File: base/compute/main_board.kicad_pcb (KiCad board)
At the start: 2 copper layers, 66.5 x 44 mm, 42 parts, among them J1 USB_C_Receptacle_USB2.0_16P, J3 Conn_02x20_Counter_Clockwise, SW1 SW_Push_Open, SW2 SW_Push_Open, U1 MCP1700T-1202ETT, U2 ESP32-S3-WROOM-2, U3 LD1117S33TR_SOT223, U4 W25X20CLSN, U5 ICE40UP5K-SG48ITR-FPGA_Lattice

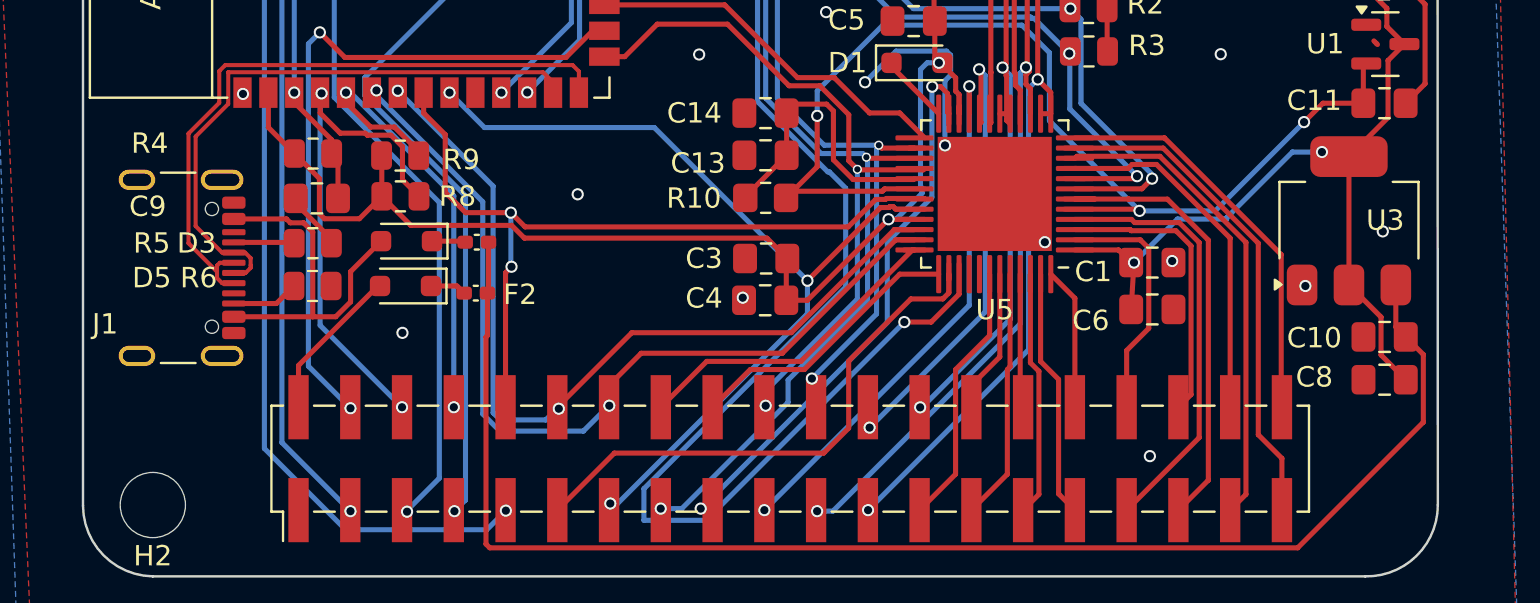
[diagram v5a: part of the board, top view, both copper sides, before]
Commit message: kicost integration for compute and extension
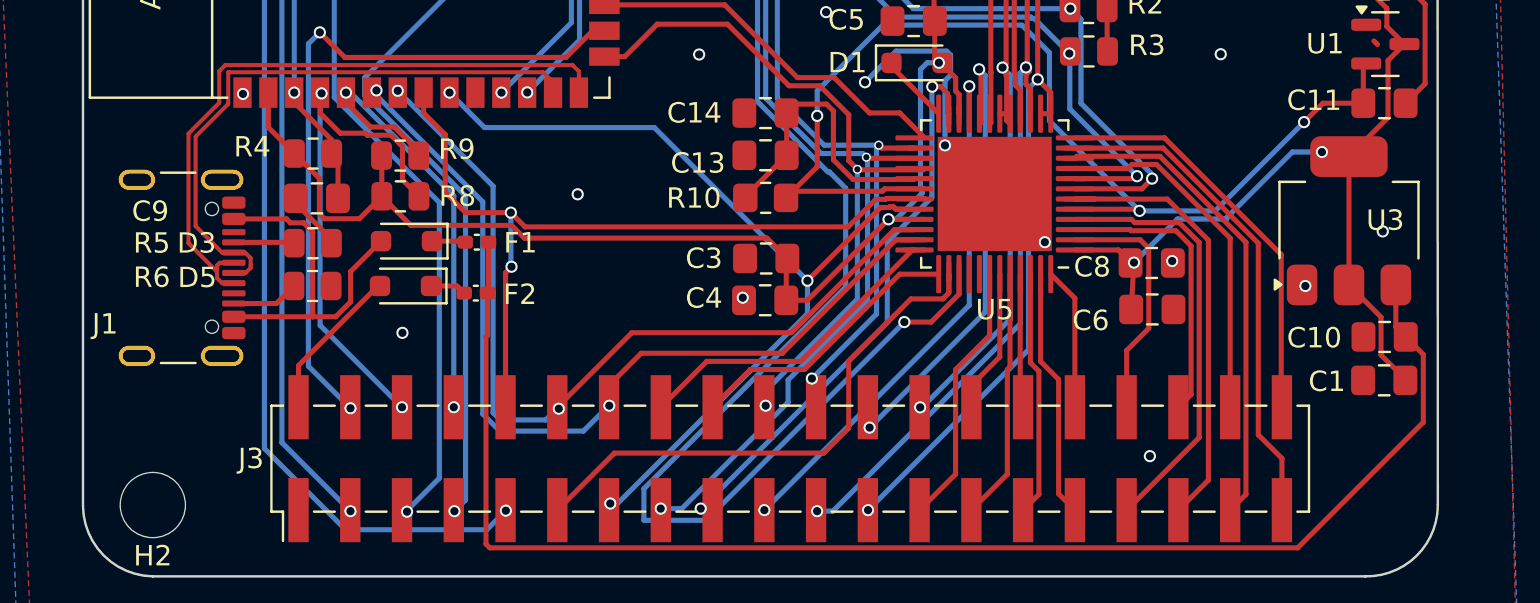
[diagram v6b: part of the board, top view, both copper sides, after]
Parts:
- moved C8 12.8 mm to (223.5, 159.1), turned to 0 degrees
- moved C1 12.8 mm to (234.9, 164.8), turned to 180 degrees
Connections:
- net FPGA41 renamed INDEX_X
- net GPIO43 renamed UART
- net GPIO44 renamed UARX
- J3 pad 1: unconnected-(J3-Pin_1-Pad1) -> GND
- J3 pad 11: HALL2 -> HALL2_old
- J3 pad 14: FPGA46 -> Z_STEP
- J3 pad 15: FPGA38 -> Z_DIR
- J3 pad 16: DIGITAL -> Y_DIR
- J3 pad 18: HALL1 -> Y_STEP
- J3 pad 19: Z_STEP -> Y_PO
- J3 pad 22: FPGA39 -> X_STEP
- J3 pad 24: Z_DIR -> X_DIR
- J3 pad 25: HALL3 -> X_PO
- J3 pad 27: uL -> FPGA3
- J3 pad 28: uH -> FPGA49
- J3 pad 29: vL -> DIGITAL
- J3 pad 30: vH -> HALL1
- J3 pad 31: wH -> HALL2
- J3 pad 32: wL -> HALL3
- J3 pad 33: X_DIR -> uH
- J3 pad 34: IC_HB_PWM1 -> uL
- J3 pad 35: X_STEP -> vH
- J3 pad 36: IC_HB_PWM2 -> vL
- J3 pad 37: Y_DIR -> wH
- J3 pad 38: X_PO -> wL
- J3 pad 39: Y_STEP -> IC_HB_PWM1
- J3 pad 40: Y_PO -> IC_HB_PWM2
- U2 pad 38: FPGA39 -> X_STEP
- U2 pad 39: FPGA38 -> Z_DIR
- U2 pad 6: FPGA46 -> Z_STEP
- U5 pad 10: Y_DIR -> wH
- U5 pad 11: Y_STEP -> IC_HB_PWM1
- U5 pad 12: Y_PO -> IC_HB_PWM2
- U5 pad 2: IC_HB_PWM1 -> uL
- U5 pad 20: Z_DIR -> X_DIR
- U5 pad 21: Z_STEP -> Y_PO
- U5 pad 26: FPGA39 -> X_STEP
- U5 pad 27: FPGA38 -> Z_DIR
- U5 pad 3: IC_HB_PWM2 -> vL
- U5 pad 35: FPGA46 -> Z_STEP
- U5 pad 36: DIGITAL -> Y_DIR
- U5 pad 37: HALL1 -> Y_STEP
- U5 pad 38: HALL2 -> HALL2_old
- U5 pad 4: X_DIR -> uH
- U5 pad 42: HALL3 -> X_PO
- U5 pad 43: uH -> FPGA49
- U5 pad 44: uL -> FPGA3
- U5 pad 45: vH -> HALL1
- U5 pad 46: vL -> DIGITAL
- U5 pad 47: wH -> HALL2
- U5 pad 48: wL -> HALL3
- U5 pad 6: X_STEP -> vH
- U5 pad 9: X_PO -> wL
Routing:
- net FPGA38: track 78.6 -> 0.00 mm, vias 3 -> 0
- net FPGA39: track 65.4 -> 0.00 mm, vias 3 -> 0
- net Z_DIR: track 22.8 -> 78.6 mm, vias 2 -> 3
- net FPGA46: track 45.3 -> 0.00 mm, vias 2 -> 0
- net X_STEP: track 22.7 -> 65.4 mm, vias 0 -> 3
- net HALL2_old: track 0.00 -> 27.2 mm
- net Z_STEP: track 26.3 -> 45.3 mm
- net vH: track 6.59 -> 22.7 mm
- net HALL2: track 27.2 -> 12.3 mm
- net uH: track 7.16 -> 21.2 mm
- net IC_HB_PWM1: track 12.0 -> 24.9 mm
- net FPGA3: track 0.00 -> 12.4 mm
- net wH: track 12.3 -> 24.1 mm
- net Y_STEP: track 24.9 -> 13.8 mm
- net wL: track 7.17 -> 18.1 mm
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
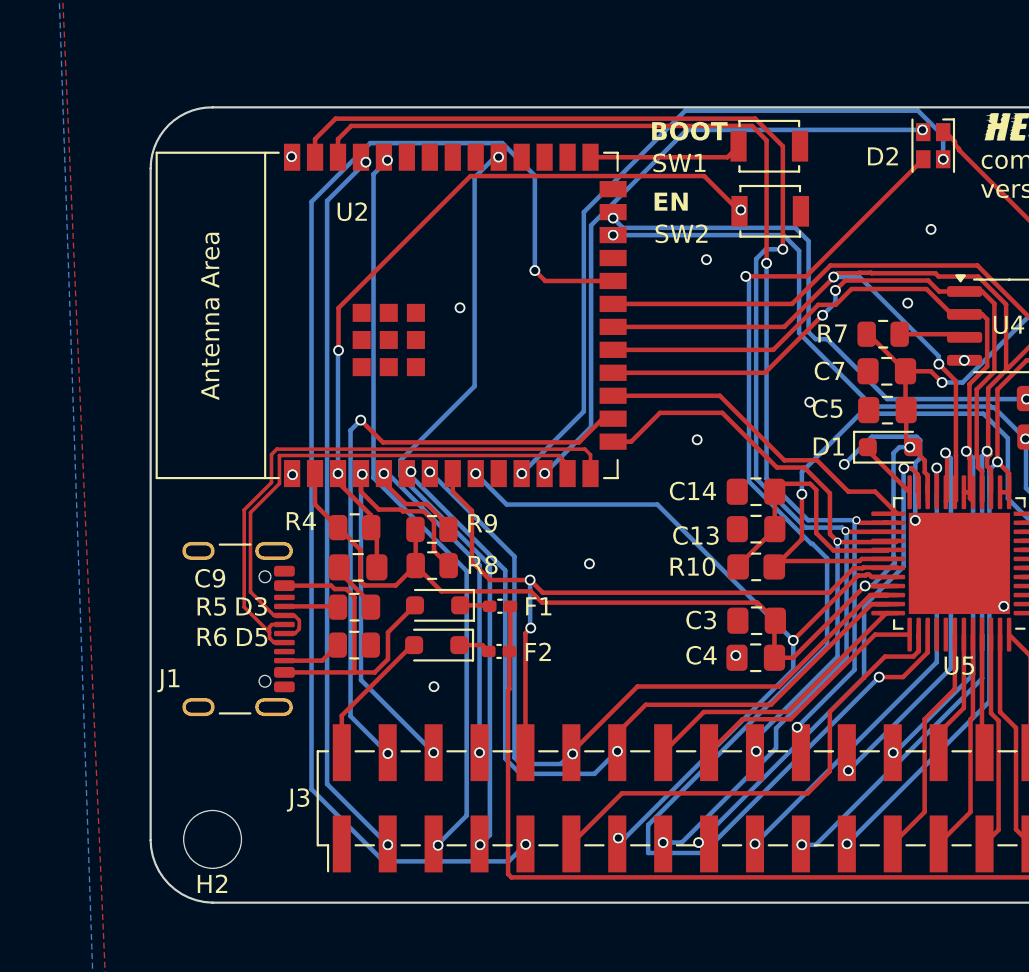
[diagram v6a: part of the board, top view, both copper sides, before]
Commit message: improved position esp32, kicost integration fix for compute module
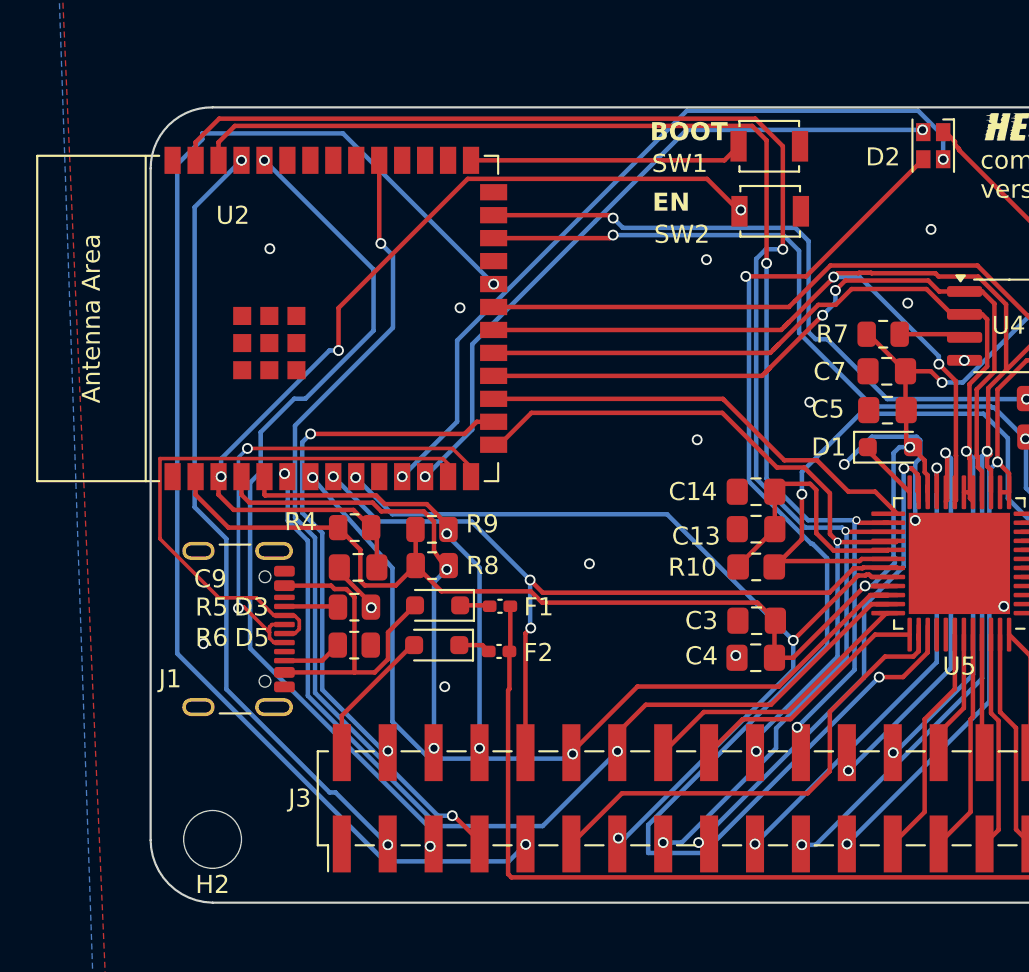
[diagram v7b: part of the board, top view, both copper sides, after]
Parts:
- moved U2 6.61 mm to (180.5, 142.1)
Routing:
- net Net-(U2-EN): track 41.6 -> 51.1 mm
- net Z_STEP: track 45.3 -> 54.7 mm
- net SPI_SI: track 52.8 -> 59.9 mm
- net SPI_SS: track 35.6 -> 42.6 mm
- net SPI_SCK: track 81.0 -> 88.0 mm
- net UARX: track 41.0 -> 47.8 mm
- net SPI_SO: track 65.6 -> 72.3 mm
- net INDEX_X: track 34.4 -> 41.0 mm
- net Net-(U2-GPIO0/BOOT): track 8.44 -> 15.1 mm
- net Z_DIR: track 78.6 -> 85.3 mm
- net X_STEP: track 65.4 -> 72.1 mm
- net CFG_RST: track 41.6 -> 48.3 mm
- net CFG_DONE: track 44.0 -> 50.6 mm
- net FPGA43: track 43.9 -> 50.4 mm
- net SPI_SS_FPGA: track 18.4 -> 25.0 mm
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
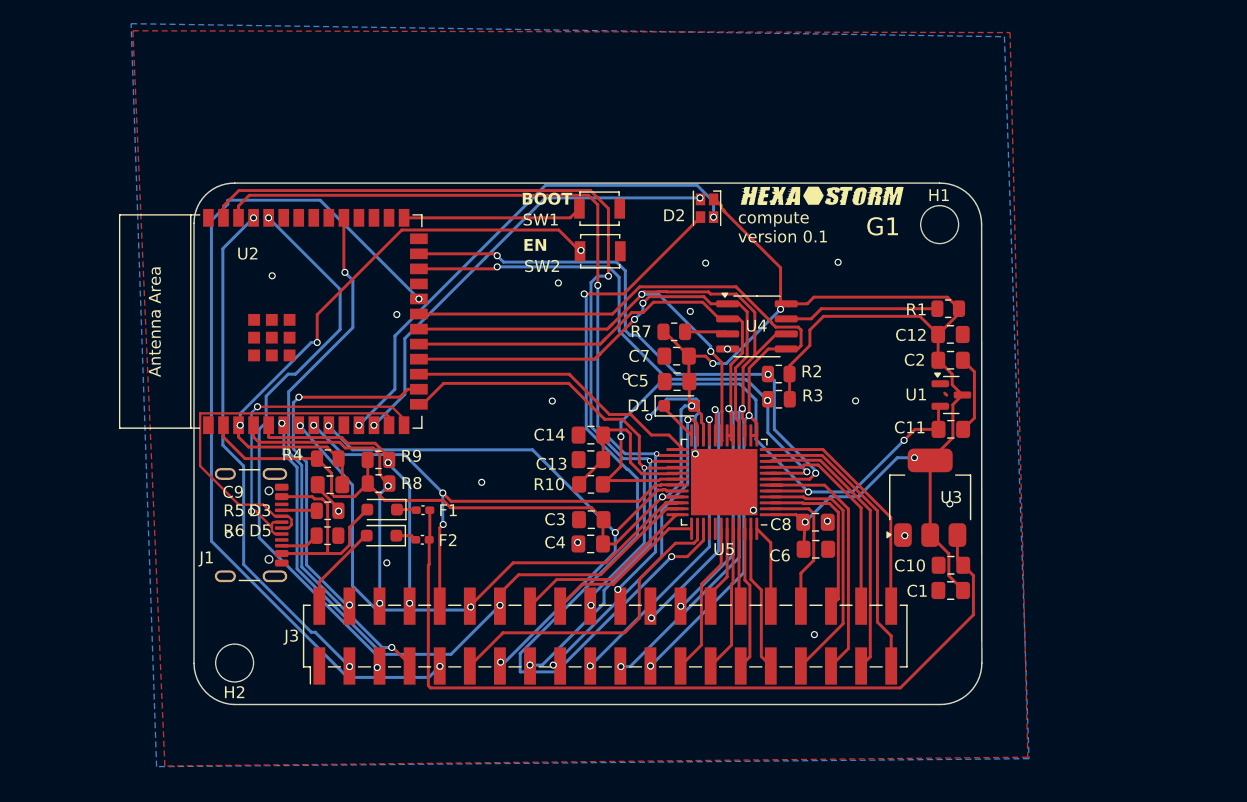
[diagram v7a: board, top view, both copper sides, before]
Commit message: fixed boms, small modifications to the boards.
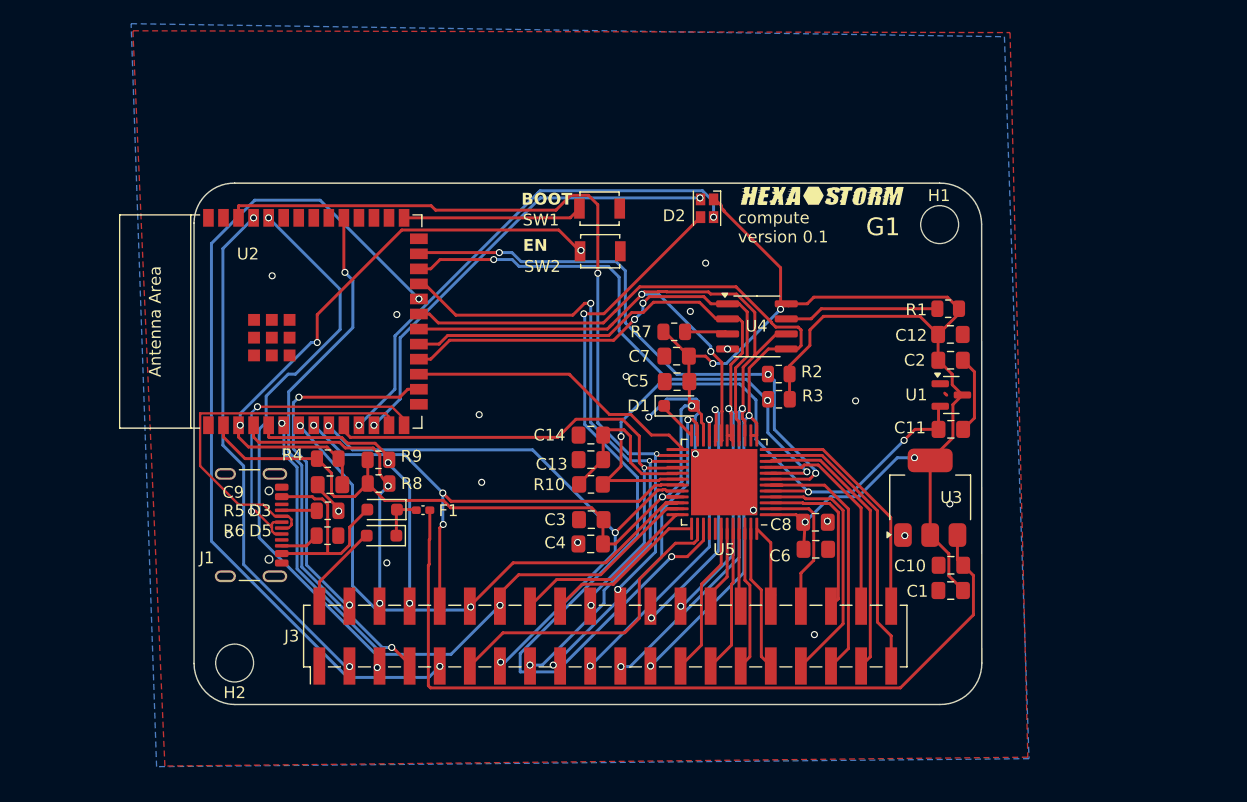
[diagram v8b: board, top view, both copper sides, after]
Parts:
- removed F2: Fuse, Fuse:Fuse_0402_1005Metric_Pad0.77x0.64mm_HandSolder
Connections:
- net HALL2_old renamed FPGA50
- net SPI_SS_MOTOR renamed GPIO14
- D3 pad 1: Net-(D3-K) -> 5Vfuse
- D5 pad 1: Net-(D5-K) -> 5Vfuse
- F1 pad 1: Net-(D3-K) -> 5Vfuse
- U2 pad 10: unconnected-(U2-GPIO17/U1TXD/ADC2_CH6-Pad10) -> INDEX_X
- U2 pad 15: INDEX_X -> unconnected-(U2-GPIO3/TOUCH3/ADC1_CH2-Pad15)
- U2 pad 23: unconnected-(U2-GPIO21-Pad23) -> Z_DIR
- U2 pad 39: Z_DIR -> unconnected-(U2-GPIO1/TOUCH1/ADC1_CH0-Pad39)
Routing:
- net Z_DIR: track 85.3 -> 57.3 mm
- net INDEX_X: track 41.0 -> 47.2 mm
- net 5Vfuse: track 0.00 -> 3.87 mm
- net Net-(D5-K): track 1.77 -> 0.00 mm
- net Net-(D3-K): track 1.65 -> 0.00 mm
- net GPIO14: track 73.6 -> 72.3 mm
- net FPGAG: track 71.8 -> 71.0 mm
- net SPI_SO: track 72.3 -> 72.9 mm
- net CFG_RST: track 48.3 -> 48.8 mm
- net GND: vias 22 -> 20
